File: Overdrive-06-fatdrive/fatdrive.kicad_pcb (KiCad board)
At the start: 2 copper layers, 62 x 46.9 mm, 46 parts, among them J1 Conn_01x04_Pin, SW1 SW_SPDT, U1 TL072, U2 TL072, U3 CD4049UB

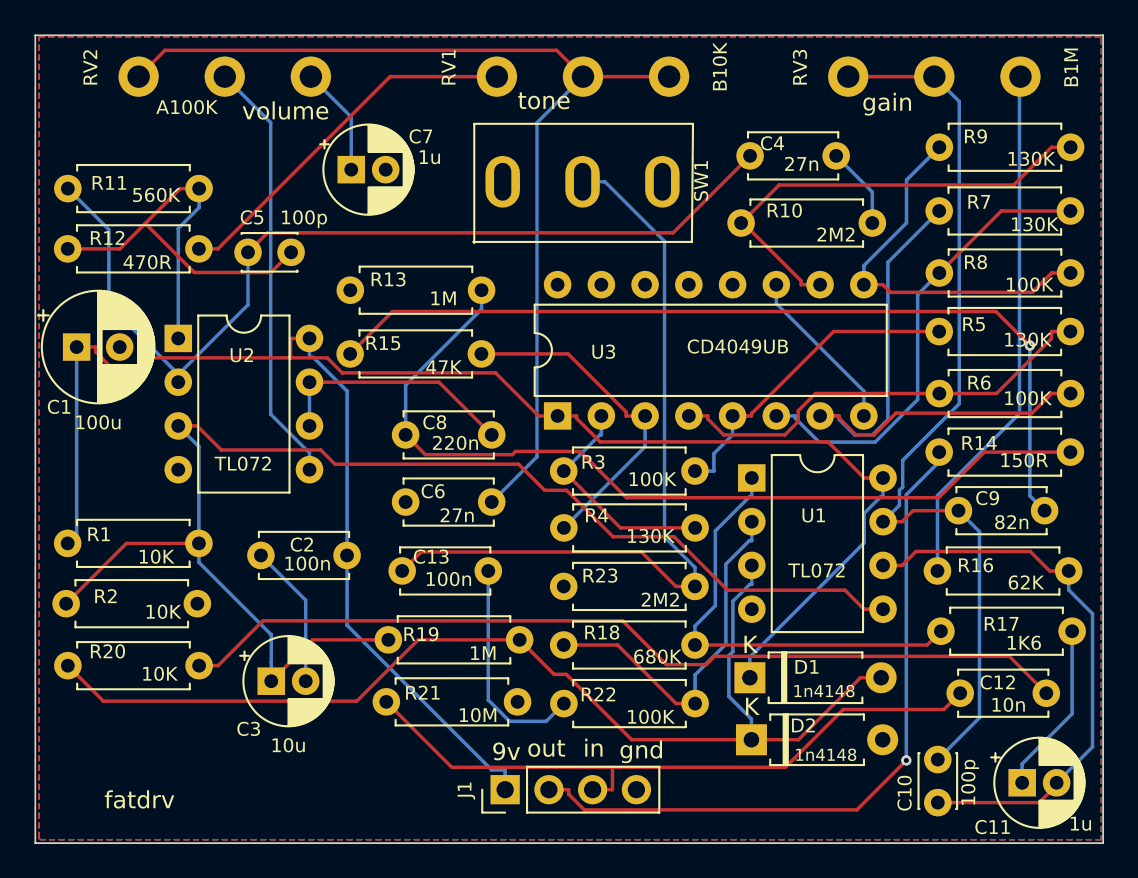
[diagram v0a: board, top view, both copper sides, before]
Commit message: re-generated the Fatdrive and badmonkey boards, as they were just a hair too large for the enclosures I am using.
x
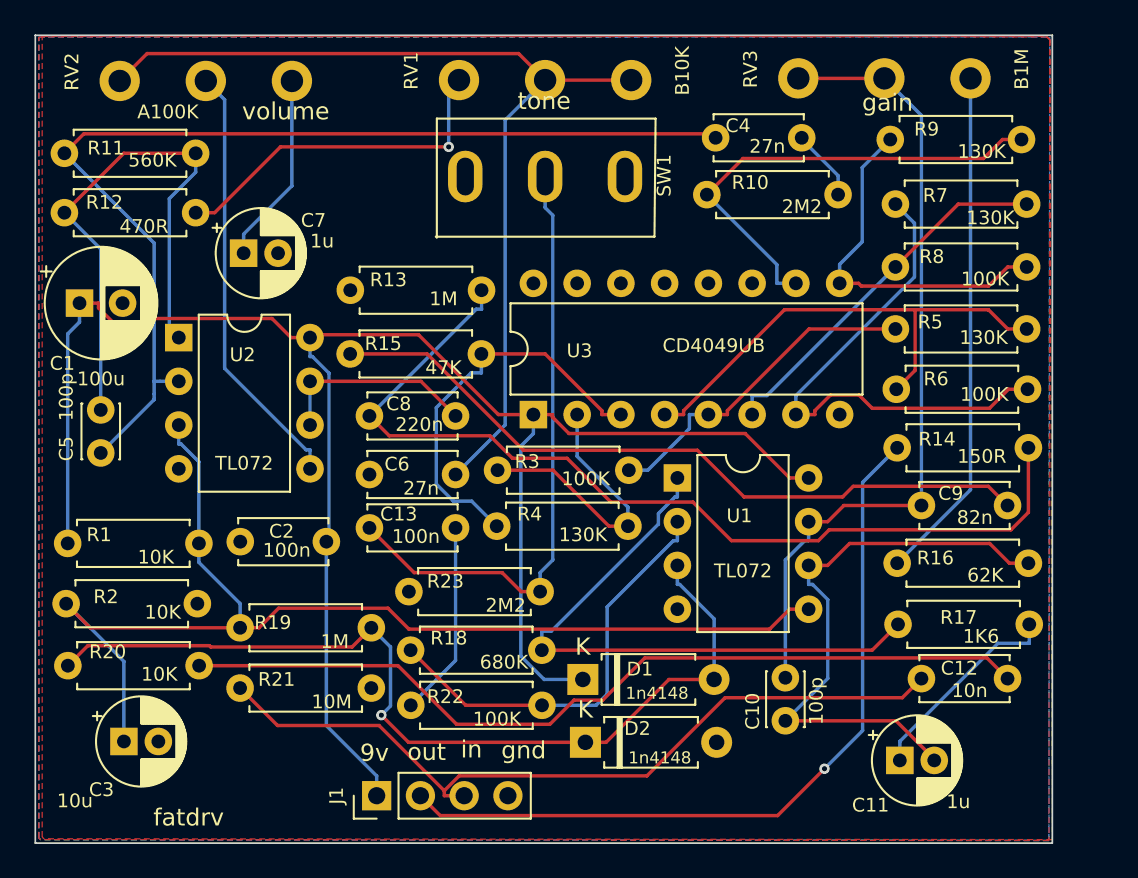
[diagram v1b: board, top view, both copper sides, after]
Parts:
- moved C5 14.5 mm to (103.8, 124.2), turned to 90 degrees
- moved C10 10.0 mm to (143.6, 139.8)
- moved D1 9.70 mm to (131.8, 137.4)
- moved D2 9.64 mm to (131.9, 141.1)
- moved C3 9.24 mm to (105.1, 141.0)
- moved R23 9.00 mm to (121.7, 132.3)
- moved R18 8.90 mm to (121.8, 135.7)
- moved R22 8.89 mm to (121.8, 138.9)
- moved R19 8.64 mm to (119.5, 134.4)
- moved R21 8.53 mm to (111.9, 137.9)
- moved C7 7.91 mm to (112.1, 112.7)
- moved J1 7.47 mm to (119.8, 144.2)
- moved C11 7.22 mm to (150.2, 142.1)
- moved U1 4.32 mm to (137.3, 125.7)
- moved R4 3.90 mm to (126.8, 128.5)
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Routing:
- net GND: track 18.8 -> 0.00 mm
- net vb: track 79.3 -> 67.9 mm
- net Net-(D1-A): track 64.7 -> 53.4 mm, vias 0 -> 1
- net Net-(SW1-B): track 45.2 -> 36.0 mm
- net Net-(R17-Pad1): track 25.8 -> 35.0 mm
- net Net-(C9-Pad2): track 51.2 -> 42.3 mm, vias 1 -> 0
- net in: track 39.1 -> 46.2 mm
- net Net-(U2A--): track 53.8 -> 60.6 mm
- net Net-(C10-Pad2): track 53.9 -> 47.4 mm
- net Net-(R7-Pad2): track 26.9 -> 21.6 mm
- net Net-(C5-Pad2): track 28.4 -> 33.3 mm
- net Net-(C7-Pad1): track 6.37 -> 11.2 mm
- net Net-(C8-Pad1): track 51.6 -> 55.9 mm
- net out: track 41.3 -> 45.4 mm
- net Net-(R6-Pad2): track 34.3 -> 30.4 mm
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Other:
- board size 62 x 46.9 mm -> 59.1 x 46.9 mm
